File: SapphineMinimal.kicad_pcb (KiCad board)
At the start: 4 copper layers, 54.6 x 61 mm, 159 parts, among them IC201 DNP DLHR-F50D-E1BD-C-NAV8, IC501 SLG59M1446V, J301 503182-1852, J401 DNP Conn_01x01_Male, J402 Conn_01x04_Male, J403 ExtPPS, J501 JST, J801 USB_B_Micro, J802 DNP Conn_02x05_Odd_Even, J803 DNP Conn_02x05_Odd_Even, J805 Conn_01x04_Male, M701 DNP AdafruitWINC1500, Q501 BC857BDW1T1G, Q502 SSM3J378R,LXHF, SW801 EVQP7C01P, SW802 EVQP7C01P, U201 LIS2HH12TR, U202 BMP390, U301 MB85RS2MTAPNF-G-BDERE1, U402 SAM-M8Q-0-10, U501 TPS62150, U801 ATSAMD21G18A-A, U802 DS3231SN

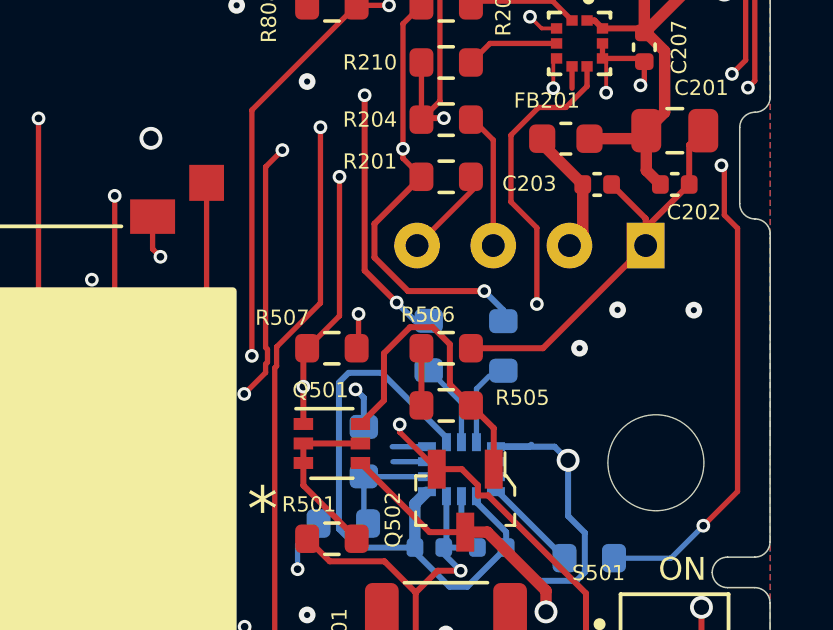
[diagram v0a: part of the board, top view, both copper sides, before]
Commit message: Updated to correct wiring of IIM42351
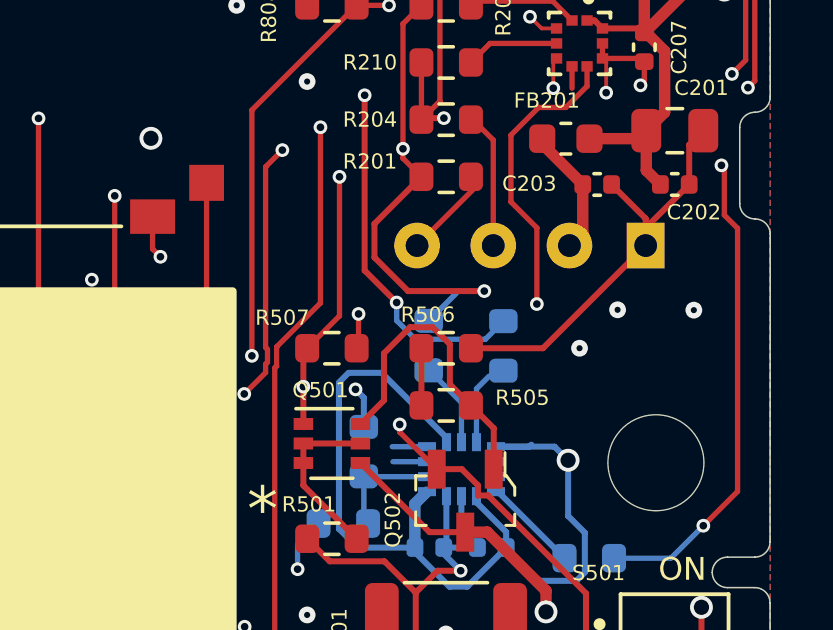
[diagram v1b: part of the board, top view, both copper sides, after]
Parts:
- R402, R403, R404, R803, R804, R805, R806: value 2K -> 1K
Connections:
- R211 pad 2: /I2C_SDA -> /I2C_SCL
- R212 pad 2: /I2C_SCL -> /I2C_SDA
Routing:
- net /I2C_SDA: track 134.5 -> 137.9 mm
- net /I2C_SCL: track 126.9 -> 127.9 mm
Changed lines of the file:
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@@
     (tags "resistor")
     (property "DPN" "490-10748-1-ND")
-    (property "Description" "2 kOhms ±1% 0.1W, 1/10W Chip Resistor 0603")
+    (property "Description" "1 kOhms ±1% 0.1W, 1/10W Chip Resistor 0603")
     (property "Digi-Key_PN" "541-3953-1-ND")
     (property "DigiKey Price" "0.05")
     (property "Distributor" "Digikey")
-    (property "MPN" "CRCW06032K00FKEAC")
+    (property "MPN" "CRCW06031K00FKEAC")
     (property "MacroFab_PN" "MF-RES-0603-2K")
     (property "Manufacturer" "Vishay")
@@
       (effects (font (size 0.508 0.508) (thickness 0.1524)))
     )
-    (fp_text value "2K" (at 0 1.43) (layer "F.Fab")
+    (fp_text value "1K" (at 0 1.43) (layer "F.Fab")
       (effects (font (size 0.508 0.508) (thickness 0.1524)))
     )
@@
     (tags "resistor")
     (property "DPN" "490-10748-1-ND")
-    (property "Description" "2 kOhms ±1% 0.1W, 1/10W Chip Resistor 0603")
+    (property "Description" "1 kOhms ±1% 0.1W, 1/10W Chip Resistor 0603")
     (property "Digi-Key_PN" "541-3953-1-ND")
     (property "DigiKey Price" "0.05")
     (property "Distributor" "Digikey")
-    (property "MPN" "CRCW06032K00FKEAC")
+    (property "MPN" "CRCW06031K00FKEAC")
     (property "MacroFab_PN" "MF-RES-0603-2K")
     (property "Manufacturer" "Vishay")
@@
       (effects (font (size 0.508 0.508) (thickness 0.1524)))
     )
-    (fp_text value "2K" (at 0 1.43) (layer "F.Fab")
+    (fp_text value "1K" (at 0 1.43) (layer "F.Fab")
       (effects (font (size 0.508 0.508) (thickness 0.1524)))
     )
@@
     (tags "resistor")
     (property "DPN" "490-10748-1-ND")
-    (property "Description" "2 kOhms ±1% 0.1W, 1/10W Chip Resistor 0603")
+    (property "Description" "1 kOhms ±1% 0.1W, 1/10W Chip Resistor 0603")
     (property "Digi-Key_PN" "541-3953-1-ND")
     (property "DigiKey Price" "0.05")
     (property "Distributor" "Digikey")
-    (property "MPN" "CRCW06032K00FKEAC")
+    (property "MPN" "CRCW06031K00FKEAC")
     (property "MacroFab_PN" "MF-RES-0603-2K")
     (property "Manufacturer" "Vishay")
@@
       (effects (font (size 0.508 0.508) (thickness 0.1524)))
     )
-    (fp_text value "2K" (at 0 1.43) (layer "F.Fab")
+    (fp_text value "1K" (at 0 1.43) (layer "F.Fab")
       (effects (font (size 0.508 0.508) (thickness 0.1524)))
     )
@@
     (tags "resistor")
     (property "DPN" "490-10748-1-ND")
-    (property "Description" "2 kOhms ±1% 0.1W, 1/10W Chip Resistor 0603")
+    (property "Description" "1 kOhms ±1% 0.1W, 1/10W Chip Resistor 0603")
     (property "Digi-Key_PN" "541-3953-1-ND")
     (property "DigiKey Price" "0.05")
     (property "Distributor" "Digikey")
-    (property "MPN" "CRCW06032K00FKEAC")
+    (property "MPN" "CRCW06031K00FKEAC")
     (property "MacroFab_PN" "MF-RES-0603-2K")
     (property "Manufacturer" "Vishay")
@@
       (effects (font (size 0.508 0.508) (thickness 0.1524)))
     )
-    (fp_text value "2K" (at 0 1.43) (layer "F.Fab")
+    (fp_text value "1K" (at 0 1.43) (layer "F.Fab")
       (effects (font (size 0.508 0.508) (thickness 0.1524)))
     )
@@
     (tags "resistor")
     (property "DPN" "490-10748-1-ND")
-    (property "Description" "2 kOhms ±1% 0.1W, 1/10W Chip Resistor 0603")
+    (property "Description" "1 kOhms ±1% 0.1W, 1/10W Chip Resistor 0603")
     (property "Digi-Key_PN" "541-3953-1-ND")
     (property "DigiKey Price" "0.05")
     (property "Distributor" "Digikey")
-    (property "MPN" "CRCW06032K00FKEAC")
+    (property "MPN" "CRCW06031K00FKEAC")
     (property "MacroFab_PN" "MF-RES-0603-2K")
     (property "Manufacturer" "Vishay")
@@
       (effects (font (size 0.508 0.508) (thickness 0.127)) (justify mirror))
     )
-    (fp_text value "2K" (at 0 -1.43) (layer "B.Fab")
+    (fp_text value "1K" (at 0 -1.43) (layer "B.Fab")
       (effects (font (size 1 1) (thickness 0.15)) (justify mirror))
     )
@@
       (net 157 "Net-(AC201-Pad13)") (pintype "passive"))
     (pad "2" smd roundrect (at 0.825 0 90) (size 0.8 0.95) (layers "B.Cu" "B.Paste" "B.Mask") (roundrect_rratio 0.25)
-      (net 123 "/I2C_SDA") (pintype "passive"))
+      (net 124 "/I2C_SCL") (pintype "passive"))
     (model "${KICAD6_3DMODEL_DIR}/Resistor_SMD.3dshapes/R_0603_1608Metric.wrl"
       (offset (xyz 0 0 0))
@@
     (tags "resistor")
     (property "DPN" "490-10748-1-ND")
-    (property "Description" "2 kOhms ±1% 0.1W, 1/10W Chip Resistor 0603")
+    (property "Description" "1 kOhms ±1% 0.1W, 1/10W Chip Resistor 0603")
     (property "Digi-Key_PN" "541-3953-1-ND")
     (property "DigiKey Price" "0.05")
     (property "Distributor" "Digikey")
-    (property "MPN" "CRCW06032K00FKEAC")
+    (property "MPN" "CRCW06031K00FKEAC")
     (property "MacroFab_PN" "MF-RES-0603-2K")
     (property "Manufacturer" "Vishay")
@@
       (effects (font (size 0.508 0.508) (thickness 0.127)) (justify mirror))
     )
-    (fp_text value "2K" (at 0 -1.43) (layer "B.Fab")
+    (fp_text value "1K" (at 0 -1.43) (layer "B.Fab")
       (effects (font (size 1 1) (thickness 0.15)) (justify mirror))
     )
@@
     (tags "resistor")
     (property "DPN" "490-10748-1-ND")
-    (property "Description" "2 kOhms ±1% 0.1W, 1/10W Chip Resistor 0603")
+    (property "Description" "1 kOhms ±1% 0.1W, 1/10W Chip Resistor 0603")
     (property "Digi-Key_PN" "541-3953-1-ND")
     (property "DigiKey Price" "0.05")
     (property "Distributor" "Digikey")
-    (property "MPN" "CRCW06032K00FKEAC")
+    (property "MPN" "CRCW06031K00FKEAC")
     (property "MacroFab_PN" "MF-RES-0603-2K")
     (property "Manufacturer" "Vishay")
@@
       (effects (font (size 0.508 0.508) (thickness 0.127)) (justify mirror))
     )
-    (fp_text value "2K" (at 0 -1.43) (layer "B.Fab")
+    (fp_text value "1K" (at 0 -1.43) (layer "B.Fab")
       (effects (font (size 1 1) (thickness 0.15)) (justify mirror))
     )
@@
       (net 158 "Net-(AC201-Pad14)") (pintype "passive"))
     (pad "2" smd roundrect (at 0.825 0 90) (size 0.8 0.95) (layers "B.Cu" "B.Paste" "B.Mask") (roundrect_rratio 0.25)
-      (net 124 "/I2C_SCL") (pintype "passive"))
+      (net 123 "/I2C_SDA") (pintype "passive"))
     (model "${KICAD6_3DMODEL_DIR}/Resistor_SMD.3dshapes/R_0603_1608Metric.wrl"
       (offset (xyz 0 0 0))
@@
     (effects (font (size 0.762 0.762) (thickness 0.1524)) (justify mirror))
   )
+  (gr_text "K" (at 78.988278 99.814618 90) (layer "B.SilkS")
+    (effects (font (size 0.52 0.52) (thickness 0.127)) (justify mirror))
+  )
   (gr_text "EN" (at 104.185078 126.484618) (layer "B.SilkS")
     (effects (font (size 0.52 0.52) (thickness 0.127)) (justify mirror))
@@
     (effects (font (size 0.52 0.52) (thickness 0.127)) (justify mirror))
   )
+  (gr_text "*" (at 124.200278 90.797618) (layer "B.SilkS")
+    (effects (font (size 0.52 0.52) (thickness 0.127)) (justify mirror))
+  )
   (gr_text "IRQ" (at 106.826678 126.433818) (layer "B.SilkS")
     (effects (font (size 0.52 0.52) (thickness 0.127)) (justify mirror))
@@
     (effects (font (size 0.52 0.52) (thickness 0.127)) (justify mirror))
   )
+  (gr_text "K" (at 77.337278 91.940618 270) (layer "B.SilkS")
+    (effects (font (size 0.52 0.52) (thickness 0.127)) (justify mirror))
+  )
   (gr_text "P3V3" (at 107.436278 116.832618 90) (layer "B.SilkS")
     (effects (font (size 0.52 0.52) (thickness 0.127)) (justify mirror))
@@
   (segment (start 113.532278 88.638618) (end 101.848278 88.638618) (width 0.1778) (layer "In1.Cu") (net 123))
   (segment (start 118.053478 79.189818) (end 118.815478 79.951818) (width 0.20066) (layer "In1.Cu") (net 123))
-  (segment (start 120.188593 86.707523) (end 119.729183 86.707523) (width 0.20066) (layer "B.Cu") (net 123))
-  (segment (start 119.729183 86.707523) (end 119.120278 86.098618) (width 0.20066) (layer "B.Cu") (net 123))
+  (segment (start 119.120278 86.702379) (end 119.120278 86.098618) (width 0.1778) (layer "B.Cu") (net 123))
+  (segment (start 122.074273 87.323423) (end 119.741322 87.323423) (width 0.1778) (layer "B.Cu") (net 123))
+  (segment (start 122.676278 86.721418) (end 122.074273 87.323423) (width 0.1778) (layer "B.Cu") (net 123))
   (segment (start 85.473278 114.300618) (end 84.068278 112.895618) (width 0.1778) (layer "B.Cu") (net 123))
   (segment (start 86.322278 114.300618) (end 85.473278 114.300618) (width 0.1778) (layer "B.Cu") (net 123))
+  (segment (start 119.741322 87.323423) (end 119.120278 86.702379) (width 0.1778) (layer "B.Cu") (net 123))
   (segment (start 119.330378 80.974718) (end 119.330378 81.291718) (width 0.1778) (layer "F.Cu") (net 124))
   (segment (start 114.814478 88.092092) (end 114.751977 88.154593) (width 0.1778) (layer "F.Cu") (net 124))
@@
   (segment (start 85.592278 93.083618) (end 89.642024 93.083618) (width 0.1778) (layer "In1.Cu") (net 124))
   (segment (start 113.479569 122.701016) (end 88.158676 122.701016) (width 0.1778) (layer "In1.Cu") (net 124))
-  (segment (start 122.676278 86.352618) (end 122.041278 85.717618) (width 0.20066) (layer "B.Cu") (net 124))
   (segment (start 85.870278 113.300618) (end 85.084278 112.514618) (width 0.1778) (layer "B.Cu") (net 124))
-  (segment (start 122.676278 86.721418) (end 122.676278 86.352618) (width 0.20066) (layer "B.Cu") (net 124))
+  (segment (start 121.178498 85.717618) (end 122.041278 85.717618) (width 0.1778) (layer "B.Cu") (net 124))
+  (segment (start 120.188593 86.707523) (end 121.178498 85.717618) (width 0.1778) (layer "B.Cu") (net 124))
   (segment (start 96.664378 112.892518) (end 94.998278 114.558618) (width 0.20066) (layer "F.Cu") (net 125))
   (segment (start 92.196278 113.187618) (end 93.567278 114.558618) (width 0.1778) (layer "F.Cu") (net 125))

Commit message: After M2 at home.  Not sure what changes are
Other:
- board text added: "Sapphire M2 c hayward 6/21/2023 Rev 5"
- board text removed: "Sapphire M2 c hayward 5/2/2023 Rev 4"
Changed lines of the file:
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@@
     (effects (font (size 0.52 0.52) (thickness 0.127)) (justify mirror))
   )
-  (gr_text "Sapphire M2\nc hayward\n5/2/2023\nRev 4" (at 86.887678 75.125818 90) (layer "B.SilkS")
+  (gr_text "Sapphire M2\nc hayward\n6/21/2023\nRev 5" (at 86.887678 75.125818 90) (layer "B.SilkS")
     (effects (font (size 1 1) (thickness 0.15)) (justify mirror))
   )
@@
   )
   (zone (net 1) (net_name "GND") (layer "F.Cu") (hatch edge 0.508)
-    (connect_pads yes (clearance 0.3048))
+    (connect_pads (clearance 0.3048))
     (min_thickness 0.254) (filled_areas_thickness no)
-    (fill yes (thermal_gap 0.508) (thermal_bridge_width 0.508))
+    (fill yes (thermal_gap 0.254) (thermal_bridge_width 0.254))
     (polygon
       (pts
